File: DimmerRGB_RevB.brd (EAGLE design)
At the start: 75 x 65 mm, 54 parts, among them CON3 CON_10X200MIL, IC2 LM5111, IC3 LM2931_ADJ, IC4 LM5111, IC5 74HC14D, IC6 PIC16F18325, Q1 N-PWR-MOSFETLFPAK, Q2 N-PWR-MOSFETLFPAK, Q3 N-PWR-MOSFETLFPAK, Q4 N-PWR-MOSFETLFPAK, SW1 ENCODER_BOURNS, SW2 ENCODER_BOURNS, X1 22-23-2051

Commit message: Worked on RBG RevB layout
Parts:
- moved R16 60.4 mm to (67.1, 29.6), turned to 90 degrees
- moved R17 60.1 mm to (67.1, 26.1), turned to 90 degrees
- moved R4 59.8 mm to (69.2, 29.5), turned to 90 degrees
- moved LED1 59.1 mm to (69.2, 26.0), turned to 270 degrees
- moved R15 52.1 mm to (61.7, 20.2)
- moved IC3 49.1 mm to (61.6, 24.8), turned to 270 degrees
- moved C3 46.8 mm to (61.6, 30.2), turned to 180 degrees
- moved D4 38.5 mm to (54.0, 23.3)
- moved D2 38.4 mm to (54.0, 24.7), turned to 0 degrees
- moved Q5 35.8 mm to (54.1, 27.3), turned to 270 degrees
- moved R6 32.0 mm to (32.4, 6.99), turned to 270 degrees
- moved R13 31.1 mm to (44.8, 14.3)
- moved R5 30.4 mm to (30.5, 6.99), turned to 270 degrees
- moved C14 30.0 mm to (44.8, 18.1), turned to 0 degrees
- moved C12 29.5 mm to (34.3, 6.99)
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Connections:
- removed net N$16: R11.1, R12.1, SW2.B, SW4.B
- new net N$20: R11.1, R12.1, SW2.B, SW4.A
- net GND: now also SW3.D, SW4.D; no longer SW3.E, SW4.E
- net N$12: now also SW4.E; no longer SW4.D
- net N$13: now also SW3.A; no longer SW3.B
- net N$14: now also SW3.B; no longer SW3.A
- net N$17: now also SW4.B; no longer SW4.A
- net N$19: now also SW3.E; no longer SW3.D
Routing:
- net +5V: track 84.1 -> 40.7 mm, vias 8 -> 4
- net ENC2PB: track 31.3 -> 1.91 mm
- net ENC1B: track 31.8 -> 7.00 mm
- net N$12: track 0.00 -> 23.0 mm
- net N$19: track 0.00 -> 17.9 mm
- net N$17: track 2.38 -> 17.4 mm
- net N$13: track 2.47 -> 17.4 mm
- net ENC2A: track 21.5 -> 7.00 mm
- net N$20: track 0.00 -> 10.1 mm
- net ENC1A: track 21.6 -> 11.7 mm
- net ENC1PB: track 11.5 -> 1.91 mm
- net N$14: track 2.38 -> 10.0 mm
- net ENC2B: track 14.9 -> 11.7 mm
- net ENC1_B: track 2.80 -> 0.00 mm
- net N$16: track 2.38 -> 0.00 mm
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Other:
- board size 75 x 65 mm -> 75 x 60 mm

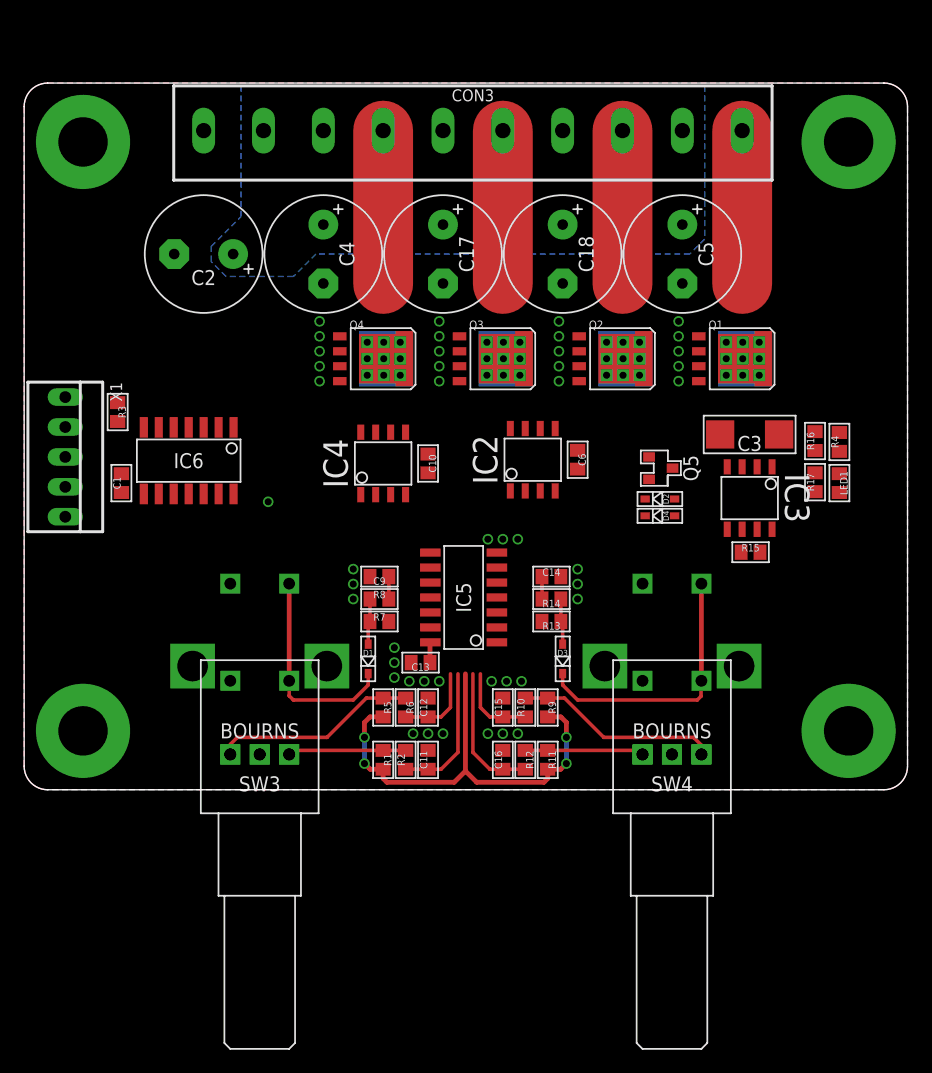
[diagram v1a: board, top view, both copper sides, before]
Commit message: Some more layouting done
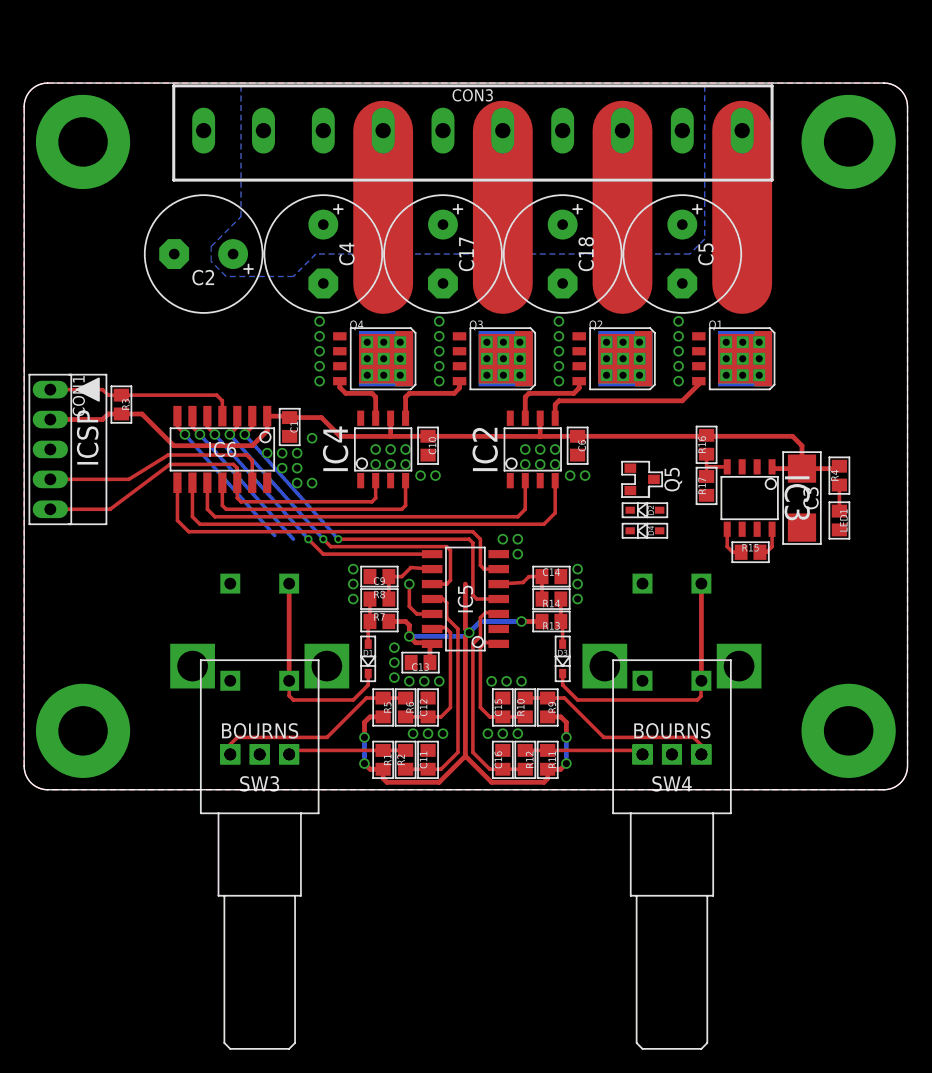
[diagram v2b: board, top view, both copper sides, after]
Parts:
- removed X1: 22-23-2051, 00Connector:22-23-2051
- added CON1: CON_5X100MIL, 00Connector:100MIL_5X
- moved C1 15.1 mm to (22.5, 30.8), turned to 270 degrees
- moved R16 9.21 mm to (57.9, 29.3)
- moved R17 9.21 mm to (57.9, 25.8)
- moved C3 6.99 mm to (66.0, 24.8), turned to 270 degrees
- moved LED1 3.18 mm to (69.2, 22.9)
- moved IC6 3.01 mm to (16.8, 28.9)
- moved R4 2.86 mm to (69.2, 26.7)
- moved Q5 1.85 mm to (52.5, 26.4)
- moved D4 1.80 mm to (52.7, 22.0)
- moved D2 1.59 mm to (52.7, 23.7)
- moved C10 1.51 mm to (34.3, 29.2)
- moved C6 1.19 mm to (47.0, 29.2)
- moved IC4 1.19 mm to (30.5, 28.9)
- moved IC2 0.87 mm to (43.2, 28.9)
- moved R3 0.71 mm to (8.26, 32.7)
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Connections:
- removed net N$21: IC6.8
- removed net N$22: IC6.2
- removed net N$23: IC6.3
- removed net N$24: IC6.5
- removed net N$25: IC6.6
- removed net N$26: IC6.7
- removed net PGC: X1.5
- removed net PGD: X1.4
- net !MCLR!: now also CON1.1; no longer X1.1
- net +5V: now also CON1.2; no longer X1.2
- net ENC1A: now also IC5.11; no longer IC5.3
- net ENC1B: now also IC5.13; no longer IC5.5
- net ENC1PB: now also IC5.9; no longer IC5.1
- net ENC1_A: now also IC5.10, IC6.3; no longer IC5.4
- net ENC1_B: now also IC5.12, IC6.6; no longer IC5.6
- net ENC1_PB: now also IC5.8, IC6.5; no longer IC5.2
- net ENC2A: now also IC5.1; no longer IC5.11
- net ENC2B: now also IC5.3; no longer IC5.13
- net ENC2PB: now also IC5.5; no longer IC5.9
- net ENC2_A: now also IC5.2, IC6.7; no longer IC5.10
- net ENC2_B: now also IC5.4, IC6.2; no longer IC5.12
- net ENC2_PB: now also IC5.6, IC6.8; no longer IC5.8
- net GND: now also CON1.3; no longer X1.3
- net PGC/OUT1: now also CON1.5
- net PGD/ENABLE: now also CON1.4
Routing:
- net +5V: track 40.7 -> 144.2 mm, vias 4 -> 7
- net OUT4: track 0.00 -> 37.1 mm
- net ENC2_PB: track 0.00 -> 33.5 mm
- net PGC/OUT1: track 0.00 -> 33.3 mm
- net OUT3: track 0.00 -> 32.2 mm
- net ENC2_B: track 0.00 -> 32.1 mm, vias 0 -> 2
- net ENC1_A: track 0.00 -> 29.2 mm, vias 0 -> 2
- net ENC1_PB: track 0.00 -> 24.8 mm, vias 0 -> 2
- net OUT2: track 0.00 -> 19.9 mm
- net PGD/ENABLE: track 0.00 -> 19.8 mm
- net ENC1_B: track 0.00 -> 17.8 mm, vias 0 -> 2
- net !MCLR!: track 0.00 -> 16.3 mm
- net N$1: track 0.00 -> 14.3 mm
- net ENC2_A: track 0.00 -> 13.3 mm, vias 0 -> 1
- net ENC1A: track 11.7 -> 19.6 mm
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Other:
- board text added: "ICSP"

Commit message: More layouting done
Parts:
- moved D2 4.69 mm to (56.8, 21.5)
- moved D4 4.69 mm to (56.8, 19.8)
- moved Q5 4.14 mm to (52.8, 22.2)
- moved C1 1.27 mm to (22.5, 32.1)
- moved CON1 1.27 mm to (2.22, 30.2)
- moved IC6 1.27 mm to (16.8, 30.2)
- moved R3 1.27 mm to (8.26, 34.0)
- moved IC2 0.32 mm to (43.2, 29.2)
- moved IC4 0.32 mm to (30.5, 29.2)
- moved C10 0.32 mm to (34.3, 29.5)
- moved C3 0.32 mm to (66.0, 25.1)
- moved C6 0.32 mm to (47.0, 29.5)
- moved IC3 0.32 mm to (61.6, 25.1)
- moved LED1 0.32 mm to (69.2, 23.2)
- moved R15 0.32 mm to (61.7, 20.5)
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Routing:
- net N$19: track 17.9 -> 56.7 mm, vias 0 -> 1
- net PGD/ENABLE: track 19.8 -> 55.4 mm, vias 0 -> 4
- net ENC2_A: track 13.3 -> 47.6 mm, vias 1 -> 4
- net +12V: track 2.70 -> 36.5 mm, vias 0 -> 1
- net ENC1_B: track 17.8 -> 37.1 mm, vias 2 -> 4
- net +5V: track 144.2 -> 157.3 mm, vias 7 -> 9
- net OUT_1: track 13.0 -> 0.20 mm
- net OUT_4: track 13.0 -> 0.20 mm
- net OUT_3: track 13.0 -> 0.20 mm
- net OUT_2: track 13.0 -> 0.20 mm
- net !ENABLE!: track 2.85 -> 11.3 mm
- net ENC1_PB: track 24.8 -> 31.7 mm
- net ENC1_A: track 29.2 -> 34.8 mm
- net ENC2_B: track 32.1 -> 37.4 mm
- net N$12: track 23.0 -> 26.8 mm
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- added copper zone on layer 1, net OUT_1
- added copper zone on layer 1, net OUT_2
- added copper zone on layer 1, net OUT_3
- added copper zone on layer 1, net OUT_4

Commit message: Final version of RGB dimmer Rev B
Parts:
- removed CON3: CON_10X200MIL, 00Connector:200MIL_10X
- added C19, C20, C21, C22, C23, C8: 100n, 00Capacitor:C0805
- added C7: 1500u, 00Capacitor:10MM
- added CON2: CON_5X100MIL, 00Connector:100MIL_5X
- C1: value 100n -> 33u; device 00Capacitor:C0805 -> 00Capacitor:SMC_C
- C11, C12: value 10n -> 100n
- C13, C14: value 100n -> 10n
- C17, C18, C2: value 1500u -> 100n; device 00Capacitor:10MM -> 00Capacitor:C0805
- C3: value 33u -> 1500u; device 00Capacitor:SMC_C -> 00Capacitor:10MM
- C6: value 100n -> 1500u; device 00Capacitor:C0805 -> 00Capacitor:10MM
- CON1: value CON_5X100MIL -> CON_10X200MIL; device 00Connector:100MIL_5X -> 00Connector:200MIL_10X
- IC2: value LM5111 -> LM2931_ADJ; device 00Logic:SOIC8 -> 00VoltageRegulator:SOIC8
- IC3: value LM2931_ADJ -> LM5111; device 00VoltageRegulator:SOIC8 -> 00Logic:SOIC8
- Q1: value N-PWR-MOSFETLFPAK -> (none); device 00Mosfet:LFPAK -> 00Mosfet:SOT23
- Q5: value (none) -> N-PWR-MOSFETLFPAK; device 00Mosfet:SOT23 -> 00Mosfet:LFPAK
- R1: value 10k -> 1k
- R10, R14, R8: value 22k -> 10k
- R13, R17, R7: value 10k -> 22k
- R15: value 33k -> 10k
- R16: value 33k -> 22k
- R2: value 22k -> 33k
- R4: value 1k -> 10k
- R5: value 10k -> 33k
- SW1, SW2: value ENCODER_BOURNS -> PEC11R
- SW3, SW4: value (none) -> PEC09
- moved R4 61.0 mm to (8.57, 34.0), turned to 270 degrees
- moved LED1 55.6 mm to (15.2, 36.5), turned to 180 degrees
- moved R3 50.5 mm to (58.1, 26.0), turned to 90 degrees
- moved CON1 47.1 mm to (38.1, 60.7), turned to 0 degrees
- moved C1 44.0 mm to (66.0, 25.7)
- moved R2 37.3 mm to (58.1, 29.5)
- moved R1 35.8 mm to (19.1, 36.5), turned to 0 degrees
- moved C6 35.5 mm to (15.2, 45.4), turned to 180 degrees
- moved R5 34.0 mm to (61.6, 20.6), turned to 0 degrees
- moved R16 30.8 mm to (30.2, 16.2), turned to 0 degrees
- moved IC3 30.4 mm to (31.4, 29.2), turned to 90 degrees
- moved D1 29.4 mm to (56.8, 21.3), turned to 0 degrees
- moved C3 28.7 mm to (45.7, 45.4)
- moved C17 27.9 mm to (30.2, 18.1), turned to 180 degrees
- moved C11 27.7 mm to (27.9, 29.5), turned to 270 degrees
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- renumbered IC6 to IC1
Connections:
- removed net N$6 (its old number): IC2.7, Q2.4
- new net N$5: IC3.7, Q2.4
- net !ENABLE!: now also D1.A, IC2.5, Q1.3, R5.1; no longer D4.A, IC3.5, Q5.3, R15.1
- net !MCLR!: now also CON2.1, R4.1; no longer CON1.1, R3.1
- net +12V: now also C3.+, C6.+, C7.+, C8.1, CON1.2, CON1.3, CON1.5, CON1.7, CON1.9, IC2.8, R5.2; no longer C17.+, C18.+, C2.+, CON3.2, CON3.3, CON3.5, CON3.7, CON3.9, IC3.8, R15.2
- net +5V: now also C1.+, C11.1, C12.1, C19.1, C2.1, C20.1, C21.1, C22.1, C23.1, C9.1, CON2.2, IC2.1, IC3.6, R10.2, R14.2, R15.2, R2.2, R8.2; no longer C1.1, C13.1, C3.+, C6.1, CON1.2, IC2.6, IC3.1, R13.2, R16.2, R3.2, R5.2, R7.2
- net ENC1A: now also C13.1, R6.1; no longer C11.1, R2.1
- net ENC1B: now also C15.1, R12.2; no longer C12.1, R6.2
- net ENC1PB: now also C17.1, R16.2; no longer C9.1, R8.2
- net ENC2A: now also C14.1, R7.1; no longer C15.1, R10.1
- net ENC2B: now also R13.2; no longer R12.2
- net ENC2PB: now also C18.1, R17.2; no longer C14.1, R14.2
- net GND: now also C1.-, C17.2, C18.2, C19.2, C2.2, C20.2, C21.2, C22.2, C23.2, C6.-, C7.-, C8.2, CON1.1, CON2.3, IC2.2, IC2.6, IC2.7, Q5.1, Q5.3, R3.1; no longer C1.2, C17.-, C18.-, C2.-, C6.2, CON1.3, CON3.1, IC3.2, IC3.6, IC3.7, Q1.1, Q1.3, R17.1
- net N$1: now also IC4.5, Q5.4; no longer IC2.5, Q1.4
- net N$11: now also IC3.5; no longer IC4.5
- net N$12: now also D2.C; no longer D3.C
- net N$13: now also R10.1, R12.1; no longer R5.1, R6.1
- net N$14: now also R6.2, R8.1; no longer R1.1, R2.2
- net N$15: now also D3.A, R14.1, R16.1; no longer D1.A, R7.1, R8.1
- net N$17: now also R7.2; no longer R10.2
- net N$18: now also D4.A, R15.1, R17.1; no longer D3.A, R13.1, R14.1
- net N$19: now also D3.C; no longer D2.C
- net N$2: now also R1.1; no longer R4.1
- net N$20: now also R13.1; no longer R12.1
- net N$8: now also IC2.4, R2.1, R3.2; no longer IC3.4, R16.1, R17.2
- net OUT2: now also IC3.4; no longer IC4.4
- net OUT3: now also IC4.2; no longer IC2.2
- net OUT4: now also IC4.4; no longer IC2.4
- net OUT_1: now also CON1.4, Q2.MB1, Q2.MB2, Q2.MB3, Q2.VIA1, Q2.VIA2, Q2.VIA3, Q2.VIA4, Q2.VIA5, Q2.VIA6, Q2.VIA7, Q2.VIA8, Q2.VIA9; no longer CON3.4, Q4.MB1, Q4.MB2, Q4.MB3, Q4.VIA1, Q4.VIA2, Q4.VIA3, Q4.VIA4, Q4.VIA5, Q4.VIA6, Q4.VIA7, Q4.VIA8, Q4.VIA9
- net OUT_2: now also CON1.6; no longer CON3.6
- net OUT_3: now also CON1.8, Q4.MB1, Q4.MB2, Q4.MB3, Q4.VIA1, Q4.VIA2, Q4.VIA3, Q4.VIA4, Q4.VIA5, Q4.VIA6, Q4.VIA7, Q4.VIA8, Q4.VIA9; no longer CON3.8, Q2.MB1, Q2.MB2, Q2.MB3, Q2.VIA1, Q2.VIA2, Q2.VIA3, Q2.VIA4, Q2.VIA5, Q2.VIA6, Q2.VIA7, Q2.VIA8, Q2.VIA9
- net OUT_4: now also CON1.10, Q5.MB1, Q5.MB2, Q5.MB3, Q5.VIA1, Q5.VIA2, Q5.VIA3, Q5.VIA4, Q5.VIA5, Q5.VIA6, Q5.VIA7, Q5.VIA8, Q5.VIA9; no longer CON3.10, Q1.MB1, Q1.MB2, Q1.MB3, Q1.VIA1, Q1.VIA2, Q1.VIA3, Q1.VIA4, Q1.VIA5, Q1.VIA6, Q1.VIA7, Q1.VIA8, Q1.VIA9
- net PGC/OUT1: now also CON2.5, IC3.2; no longer CON1.5, IC4.2
- net PGD/ENABLE: now also CON2.4, Q1.1; no longer CON1.4, Q5.1
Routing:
- net N$6 (its old number): track 6.96 -> 0.00 mm
- net N$5: track 0.00 -> 6.58 mm
- net N$1: track 14.0 -> 8.59 mm
- net OUT3: track 33.0 -> 37.5 mm
- net +5V: track 157.3 -> 161.6 mm
- net OUT4: track 37.9 -> 41.5 mm
- net +12V: track 36.5 -> 39.1 mm, vias 1 -> 3
- net N$6: track 5.39 -> 4.04 mm
- net ENC1_B: track 37.1 -> 35.8 mm
- net ENC2_PB: track 34.4 -> 33.2 mm
- net ENC2_A: track 47.6 -> 46.7 mm
- net ENC1_PB: track 31.7 -> 30.8 mm
- net N$11: track 6.96 -> 6.24 mm
- net N$13: track 17.4 -> 18.0 mm
- net N$20: track 10.1 -> 10.8 mm
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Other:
- board size 75 x 60 mm -> 75 x 65 mm
- board text added: "+ -"
- board text added: "- +"
- board text added: "6-26V"
- board text added: "Ch1"
- board text added: "Ch2"
- board text added: "Ch3"
- board text added: "Ch4"
- board text added: "January 2017 - Rev B"
- board text added: "Lukas Fässler"
- board text added: "Programmable 4-Channel Dimmer"
- board text added: "Programmable Dimmer"
- board text added: "soldernerd.com"
